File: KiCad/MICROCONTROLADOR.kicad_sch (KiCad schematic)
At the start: 18 parts, among them J3 Screw_Terminal_01x05, SW8 SW_Push, U9 PIC24HJ64GP504-I/PT, Y1 8 MHz

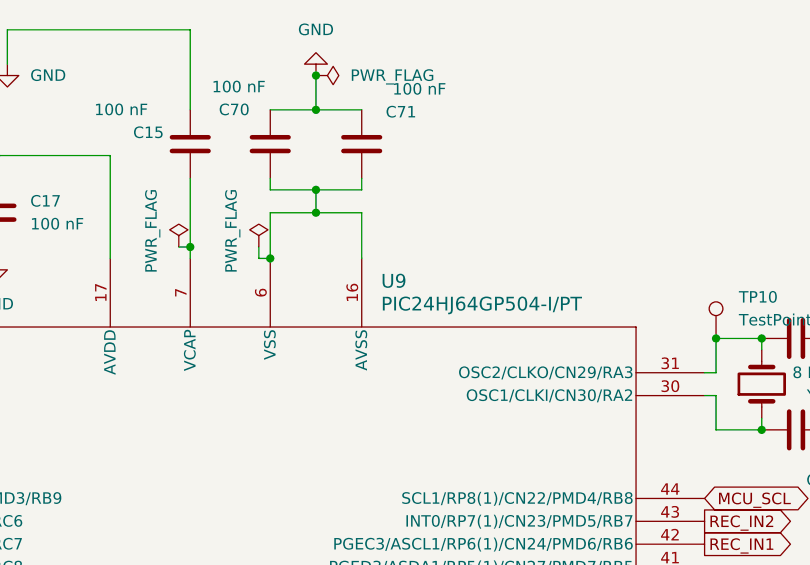
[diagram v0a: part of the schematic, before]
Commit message: Modificat ETIQUETES MICROCONTROLADOR i errors varis
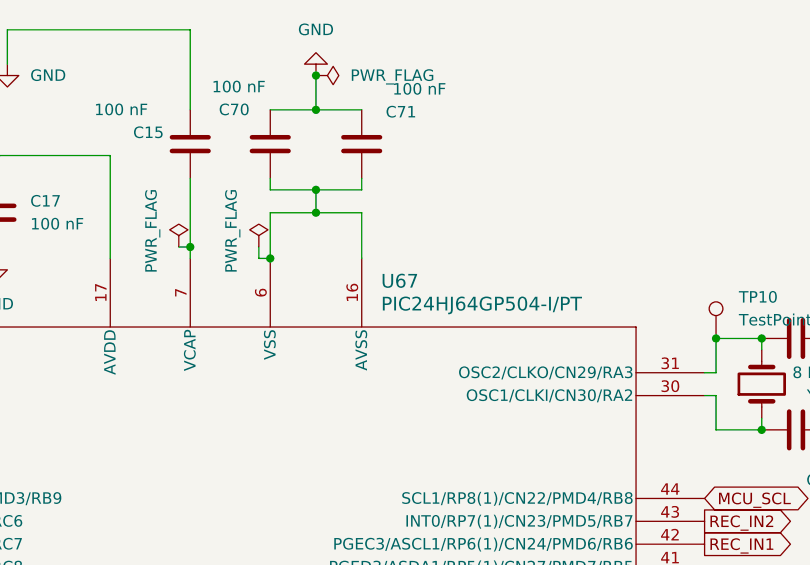
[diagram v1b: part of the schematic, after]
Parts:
- renumbered U9 to U67
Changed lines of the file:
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@@
 		(dnp no)
 		(fields_autoplaced yes)
-		(property "Reference" "U9"
+		(property "Reference" "U67"
 			(at 169.7833 44.45 0)
 			(effects
@@
 			(project "SEIENTS_EDD"
 				(path "/b6401b4f-5426-49b8-bb2e-8ecdb19989ef/2352108e-71c7-4bd2-90ee-aa6ba1d65197"
-					(reference "U9")
+					(reference "U67")
 					(unit 1)
 				)

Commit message: Modificació al placement
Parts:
- renumbered C11 to C1, C14 to C2, C15 to C3, C72 to C4, C16 to C41, C17 to C42, C73 to C5, C23 to C53, C24 to C54, C71 to C6, C70 to C7, J3 to J1, R13 to R1, R100 to R2, SW8 to SW1, TP10 to TP1, U67 to U2
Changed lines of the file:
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@@
 	(paper "A4")
 	(junction
+		(at 139.7 41.91)
+		(diameter 0)
+		(color 0 0 0 0)
+	)
+	(junction
 		(at 212.09 60.96)
 		(diameter 0)
@@
 		(dnp no)
 		(fields_autoplaced yes)
-		(property "Reference" "J3"
+		(property "Reference" "J1"
 			(at 55.88 68.58 90)
 			(effects
@@
 		(on_board yes)
 		(dnp no)
-		(property "Reference" "#FLG02"
+		(property "Reference" "#FLG0103"
 			(at 147.32 38.735 0)
 			(effects
@@
 		)
 		(instances
+			(project "MICROCONTROLADOR"
+				(path "/9b2329e0-99c8-4c5f-bbda-c735127483a8"
+					(reference "#FLG0103")
+					(unit 1)
+				)
+			)
 			(project "SEIENTS_EDD"
 				(path "/b6401b4f-5426-49b8-bb2e-8ecdb19989ef/2352108e-71c7-4bd2-90ee-aa6ba1d65197"
@@
 		(on_board yes)
 		(dnp no)
-		(property "Reference" "C14"
+		(property "Reference" "C2"
 			(at 217.932 46.736 90)
 			(effects
@@
 		(dnp no)
 		(fields_autoplaced yes)
-		(property "Reference" "TP10"
+		(property "Reference" "TP1"
 			(at 209.55 46.2279 0)
 			(effects
@@
 		(dnp no)
 		(fields_autoplaced yes)
-		(property "Reference" "R13"
+		(property "Reference" "R1"
 			(at 72.39 102.87 90)
 			(effects
@@
 		(dnp no)
 		(fields_autoplaced yes)
-		(property "Reference" "#PWR0103"
+		(property "Reference" "#PWR010"
 			(at 162.56 15.24 0)
 			(effects
@@
 		(dnp no)
 		(fields_autoplaced yes)
-		(property "Reference" "#PWR023"
+		(property "Reference" "#PWR05"
 			(at 63.5 97.79 0)
 			(effects
@@
 		(on_board yes)
 		(dnp no)
-		(property "Reference" "C24"
+		(property "Reference" "C54"
 			(at 148.336 161.29 0)
 			(effects
@@
 		(dnp no)
 		(fields_autoplaced yes)
-		(property "Reference" "C16"
+		(property "Reference" "C41"
 			(at 114.3 35.5599 0)
 			(effects
@@
 		(dnp no)
 		(fields_autoplaced yes)
-		(property "Reference" "#PWR034"
+		(property "Reference" "#PWR04"
 			(at 127 48.26 0)
 			(effects
@@
 		(on_board yes)
 		(dnp no)
-		(property "Reference" "C71"
+		(property "Reference" "C6"
 			(at 173.736 25.654 0)
 			(effects
@@
 		(dnp no)
 		(fields_autoplaced yes)
-		(property "Reference" "#PWR037"
+		(property "Reference" "#PWR08"
 			(at 140.97 171.45 0)
 			(effects
@@
 		(on_board yes)
 		(dnp no)
-		(property "Reference" "C73"
+		(property "Reference" "C5"
 			(at 173.736 156.21 0)
 			(effects
@@
 		(dnp no)
 		(fields_autoplaced yes)
-		(property "Reference" "#FLG0101"
+		(property "Reference" "#FLG0102"
 			(at 164.465 21.59 0)
 			(effects
@@
 		)
 		(instances
+			(project "MICROCONTROLADOR"
+				(path "/9b2329e0-99c8-4c5f-bbda-c735127483a8"
+					(reference "#FLG0102")
+					(unit 1)
+				)
+			)
 			(project "SEIENTS_EDD"
 				(path "/b6401b4f-5426-49b8-bb2e-8ecdb19989ef/2352108e-71c7-4bd2-90ee-aa6ba1d65197"
@@
 		(dnp no)
 		(fields_autoplaced yes)
-		(property "Reference" "R100"
+		(property "Reference" "R2"
 			(at 238.76 69.8499 0)
 			(effects
@@
 	)
 	(symbol
+		(lib_id "power:PWR_FLAG")
+		(at 139.7 41.91 90)
+		(unit 1)
+		(exclude_from_sim no)
+		(in_bom yes)
+		(on_board yes)
+		(dnp no)
+		(property "Reference" "#FLG02"
+			(at 137.795 41.91 0)
+			(effects
+				(font
+					(size 1.27 1.27)
+				)
+				(hide yes)
+			)
+		)
+		(property "Value" "PWR_FLAG"
+			(at 134.366 43.942 90)
+			(effects
+				(font
+					(size 1.27 1.27)
+				)
+			)
+		)
+		(property "Footprint" ""
+			(at 139.7 41.91 0)
+			(effects
+				(font
+					(size 1.27 1.27)
+				)
+				(hide yes)
+			)
+		)
+		(property "Datasheet" "~"
+			(at 139.7 41.91 0)
+			(effects
+				(font
+					(size 1.27 1.27)
+				)
+				(hide yes)
+			)
+		)
+		(property "Description" "Special symbol for telling ERC where power comes from"
+			(at 139.7 41.91 0)
+			(effects
+				(font
+					(size 1.27 1.27)
+				)
+				(hide yes)
+			)
+		)
+		(pin "1"
+		)
+		(instances
+			(project "MICROCONTROLADOR"
+				(path "/9b2329e0-99c8-4c5f-bbda-c735127483a8"
+					(reference "#FLG02")
+					(unit 1)
+				)
+			)
+		)
+	)
+	(symbol
 		(lib_id "power:GND")
 		(at 220.98 50.8 90)
@@
 		(dnp no)
 		(fields_autoplaced yes)
-		(property "Reference" "#PWR025"
+		(property "Reference" "#PWR02"
 			(at 227.33 50.8 0)
 			(effects
@@
 		(on_board yes)
 		(dnp no)
-		(property "Reference" "C70"
+		(property "Reference" "C7"
 			(at 155.194 25.4 0)
 			(effects
@@
 		(dnp no)
 		(fields_autoplaced yes)
-		(property "Reference" "#PWR0105"
+		(property "Reference" "#PWR09"
 			(at 165.1 171.45 0)
 			(effects
@@
 		(on_board yes)
 		(dnp no)
-		(property "Reference" "#FLG04"
+		(property "Reference" "#FLG0101"
 			(at 156.21 38.735 0)
 			(effects
@@
 		)
 		(instances
+			(project "MICROCONTROLADOR"
+				(path "/9b2329e0-99c8-4c5f-bbda-c735127483a8"
+					(reference "#FLG0101")
+					(unit 1)
+				)
+			)
 			(project "SEIENTS_EDD"
 				(path "/b6401b4f-5426-49b8-bb2e-8ecdb19989ef/2352108e-71c7-4bd2-90ee-aa6ba1d65197"
@@
 		(dnp no)
 		(fields_autoplaced yes)
-		(property "Reference" "U67"
+		(property "Reference" "U2"
 			(at 169.7833 44.45 0)
 			(effects
@@
 		(on_board yes)
 		(dnp no)
-		(property "Reference" "#FLG01"
+		(property "Reference" "#FLG03"
 			(at 133.985 149.86 0)
 			(effects
@@
 		(dnp no)
 		(fields_autoplaced yes)
-		(property "Reference" "#PWR022"
+		(property "Reference" "#PWR06"
 			(at 48.26 130.81 0)
 			(effects
@@
 		(on_board yes)
 		(dnp no)
-		(property "Reference" "C23"
+		(property "Reference" "C53"
 			(at 128.27 155.702 0)
 			(effects
@@
 		(on_board yes)
 		(dnp no)
-		(property "Reference" "C15"
+		(property "Reference" "C3"
 			(at 142.24 27.94 0)
 			(effects
@@
 		(dnp no)
 		(fields_autoplaced yes)
-		(property "Reference" "#PWR033"
+		(property "Reference" "#PWR03"
 			(at 110.49 48.26 0)
 			(effects
@@
 		(dnp no)
 		(fields_autoplaced yes)
-		(property "Reference" "#PWR0104"
+		(property "Reference" "#PWR07"
 			(at 128.27 26.67 0)
 			(effects
@@
 		(on_board yes)
 		(dnp no)
-		(property "Reference" "SW8"
+		(property "Reference" "SW1"
 			(at 59.69 118.872 0)
 			(effects
@@
 		(dnp no)
 		(fields_autoplaced yes)
-		(property "Reference" "C17"
+		(property "Reference" "C42"
 			(at 130.81 35.5599 0)
 			(effects
@@
 		(on_board yes)
 		(dnp no)
-		(property "Reference" "C72"
+		(property "Reference" "C4"
 			(at 155.194 152.654 0)
 			(effects
@@
 		(dnp no)
 		(fields_autoplaced yes)
-		(property "Reference" "#PWR024"
+		(property "Reference" "#PWR01"
 			(at 227.33 60.96 0)
 			(effects
@@
 		(on_board yes)
 		(dnp no)
-		(property "Reference" "#FLG0102"
+		(property "Reference" "#FLG01"
 			(at 172.085 149.86 0)
 			(effects
@@
 		(on_board yes)
 		(dnp no)
-		(property "Reference" "C11"
+		(property "Reference" "C1"
 			(at 220.472 66.548 90)
 			(effects

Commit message: Modificació al placement
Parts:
- renumbered C1 to C11, C2 to C14, C3 to C15, C41 to C16, C42 to C17, C53 to C23, C54 to C24, C7 to C70, C6 to C71, C4 to C72, C5 to C73, J1 to J3, R2 to R100, R1 to R13, SW1 to SW8, TP1 to TP10, U2 to U67
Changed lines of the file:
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@@
 	(paper "A4")
 	(junction
-		(at 139.7 41.91)
-		(diameter 0)
-		(color 0 0 0 0)
-	)
-	(junction
 		(at 212.09 60.96)
 		(diameter 0)
@@
 		(dnp no)
 		(fields_autoplaced yes)
-		(property "Reference" "J1"
+		(property "Reference" "J3"
 			(at 55.88 68.58 90)
 			(effects
@@
 		(on_board yes)
 		(dnp no)
-		(property "Reference" "#FLG0103"
+		(property "Reference" "#FLG02"
 			(at 147.32 38.735 0)
 			(effects
@@
 		(on_board yes)
 		(dnp no)
-		(property "Reference" "C2"
+		(property "Reference" "C14"
 			(at 217.932 46.736 90)
 			(effects
@@
 		(dnp no)
 		(fields_autoplaced yes)
-		(property "Reference" "TP1"
+		(property "Reference" "TP10"
 			(at 209.55 46.2279 0)
 			(effects
@@
 		(dnp no)
 		(fields_autoplaced yes)
-		(property "Reference" "R1"
+		(property "Reference" "R13"
 			(at 72.39 102.87 90)
 			(effects
@@
 		(dnp no)
 		(fields_autoplaced yes)
-		(property "Reference" "#PWR010"
+		(property "Reference" "#PWR0103"
 			(at 162.56 15.24 0)
 			(effects
@@
 		(dnp no)
 		(fields_autoplaced yes)
-		(property "Reference" "#PWR05"
+		(property "Reference" "#PWR023"
 			(at 63.5 97.79 0)
 			(effects
@@
 		(on_board yes)
 		(dnp no)
-		(property "Reference" "C54"
+		(property "Reference" "C24"
 			(at 148.336 161.29 0)
 			(effects
@@
 		(dnp no)
 		(fields_autoplaced yes)
-		(property "Reference" "C41"
+		(property "Reference" "C16"
 			(at 114.3 35.5599 0)
 			(effects
@@
 		(dnp no)
 		(fields_autoplaced yes)
-		(property "Reference" "#PWR04"
+		(property "Reference" "#PWR034"
 			(at 127 48.26 0)
 			(effects
@@
 		(on_board yes)
 		(dnp no)
-		(property "Reference" "C6"
+		(property "Reference" "C71"
 			(at 173.736 25.654 0)
 			(effects
@@
 		(dnp no)
 		(fields_autoplaced yes)
-		(property "Reference" "#PWR08"
+		(property "Reference" "#PWR037"
 			(at 140.97 171.45 0)
 			(effects
@@
 		(on_board yes)
 		(dnp no)
-		(property "Reference" "C5"
+		(property "Reference" "C73"
 			(at 173.736 156.21 0)
 			(effects
@@
 		(dnp no)
 		(fields_autoplaced yes)
-		(property "Reference" "#FLG0102"
+		(property "Reference" "#FLG0101"
 			(at 164.465 21.59 0)
 			(effects
@@
 		(dnp no)
 		(fields_autoplaced yes)
-		(property "Reference" "R2"
+		(property "Reference" "R100"
 			(at 238.76 69.8499 0)
 			(effects
@@
 	)
 	(symbol
-		(lib_id "power:PWR_FLAG")
-		(at 139.7 41.91 90)
-		(unit 1)
-		(exclude_from_sim no)
-		(in_bom yes)
-		(on_board yes)
-		(dnp no)
-		(property "Reference" "#FLG02"
-			(at 137.795 41.91 0)
-			(effects
-				(font
-					(size 1.27 1.27)
-				)
-				(hide yes)
-			)
-		)
-		(property "Value" "PWR_FLAG"
-			(at 134.366 43.942 90)
-			(effects
-				(font
-					(size 1.27 1.27)
-				)
-			)
-		)
-		(property "Footprint" ""
-			(at 139.7 41.91 0)
-			(effects
-				(font
-					(size 1.27 1.27)
-				)
-				(hide yes)
-			)
-		)
-		(property "Datasheet" "~"
-			(at 139.7 41.91 0)
-			(effects
-				(font
-					(size 1.27 1.27)
-				)
-				(hide yes)
-			)
-		)
-		(property "Description" "Special symbol for telling ERC where power comes from"
-			(at 139.7 41.91 0)
-			(effects
-				(font
-					(size 1.27 1.27)
-				)
-				(hide yes)
-			)
-		)
-		(pin "1"
-		)
-		(instances
-			(project "MICROCONTROLADOR"
-				(path "/9b2329e0-99c8-4c5f-bbda-c735127483a8"
-					(reference "#FLG02")
-					(unit 1)
-				)
-			)
-		)
-	)
-	(symbol
 		(lib_id "power:GND")
 		(at 220.98 50.8 90)
@@
 		(dnp no)
 		(fields_autoplaced yes)
-		(property "Reference" "#PWR02"
+		(property "Reference" "#PWR025"
 			(at 227.33 50.8 0)
 			(effects
@@
 		(on_board yes)
 		(dnp no)
-		(property "Reference" "C7"
+		(property "Reference" "C70"
 			(at 155.194 25.4 0)
 			(effects
@@
 		(dnp no)
 		(fields_autoplaced yes)
-		(property "Reference" "#PWR09"
+		(property "Reference" "#PWR0105"
 			(at 165.1 171.45 0)
 			(effects
@@
 		(on_board yes)
 		(dnp no)
-		(property "Reference" "#FLG0101"
+		(property "Reference" "#FLG04"
 			(at 156.21 38.735 0)
 			(effects
@@
 		(dnp no)
 		(fields_autoplaced yes)
-		(property "Reference" "U2"
+		(property "Reference" "U67"
 			(at 169.7833 44.45 0)
 			(effects
@@
 		(on_board yes)
 		(dnp no)
-		(property "Reference" "#FLG03"
+		(property "Reference" "#FLG01"
 			(at 133.985 149.86 0)
 			(effects
@@
 		(dnp no)
 		(fields_autoplaced yes)
-		(property "Reference" "#PWR06"
+		(property "Reference" "#PWR022"
 			(at 48.26 130.81 0)
 			(effects
@@
 		(on_board yes)
 		(dnp no)
-		(property "Reference" "C53"
+		(property "Reference" "C23"
 			(at 128.27 155.702 0)
 			(effects
@@
 		(on_board yes)
 		(dnp no)
-		(property "Reference" "C3"
+		(property "Reference" "C15"
 			(at 142.24 27.94 0)
 			(effects
@@
 		(dnp no)
 		(fields_autoplaced yes)
-		(property "Reference" "#PWR03"
+		(property "Reference" "#PWR033"
 			(at 110.49 48.26 0)
 			(effects
@@
 		(dnp no)
 		(fields_autoplaced yes)
-		(property "Reference" "#PWR07"
+		(property "Reference" "#PWR0104"
 			(at 128.27 26.67 0)
 			(effects
@@
 		(on_board yes)
 		(dnp no)
-		(property "Reference" "SW1"
+		(property "Reference" "SW8"
 			(at 59.69 118.872 0)
 			(effects
@@
 		(dnp no)
 		(fields_autoplaced yes)
-		(property "Reference" "C42"
+		(property "Reference" "C17"
 			(at 130.81 35.5599 0)
 			(effects
@@
 		(on_board yes)
 		(dnp no)
-		(property "Reference" "C4"
+		(property "Reference" "C72"
 			(at 155.194 152.654 0)
 			(effects
@@
 		(dnp no)
 		(fields_autoplaced yes)
-		(property "Reference" "#PWR01"
+		(property "Reference" "#PWR024"
 			(at 227.33 60.96 0)
 			(effects
@@
 		(on_board yes)
 		(dnp no)
-		(property "Reference" "#FLG01"
+		(property "Reference" "#FLG0102"
 			(at 172.085 149.86 0)
 			(effects
@@
 		(on_board yes)
 		(dnp no)
-		(property "Reference" "C1"
+		(property "Reference" "C11"
 			(at 220.472 66.548 90)
 			(effects
